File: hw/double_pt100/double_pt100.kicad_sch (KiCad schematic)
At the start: 30 parts, among them SW1 SW_Push, U1 WeMos_D1_mini, U2 OLED_091_module, U3 MAX31865_breakout, U4 MAX31865_breakout

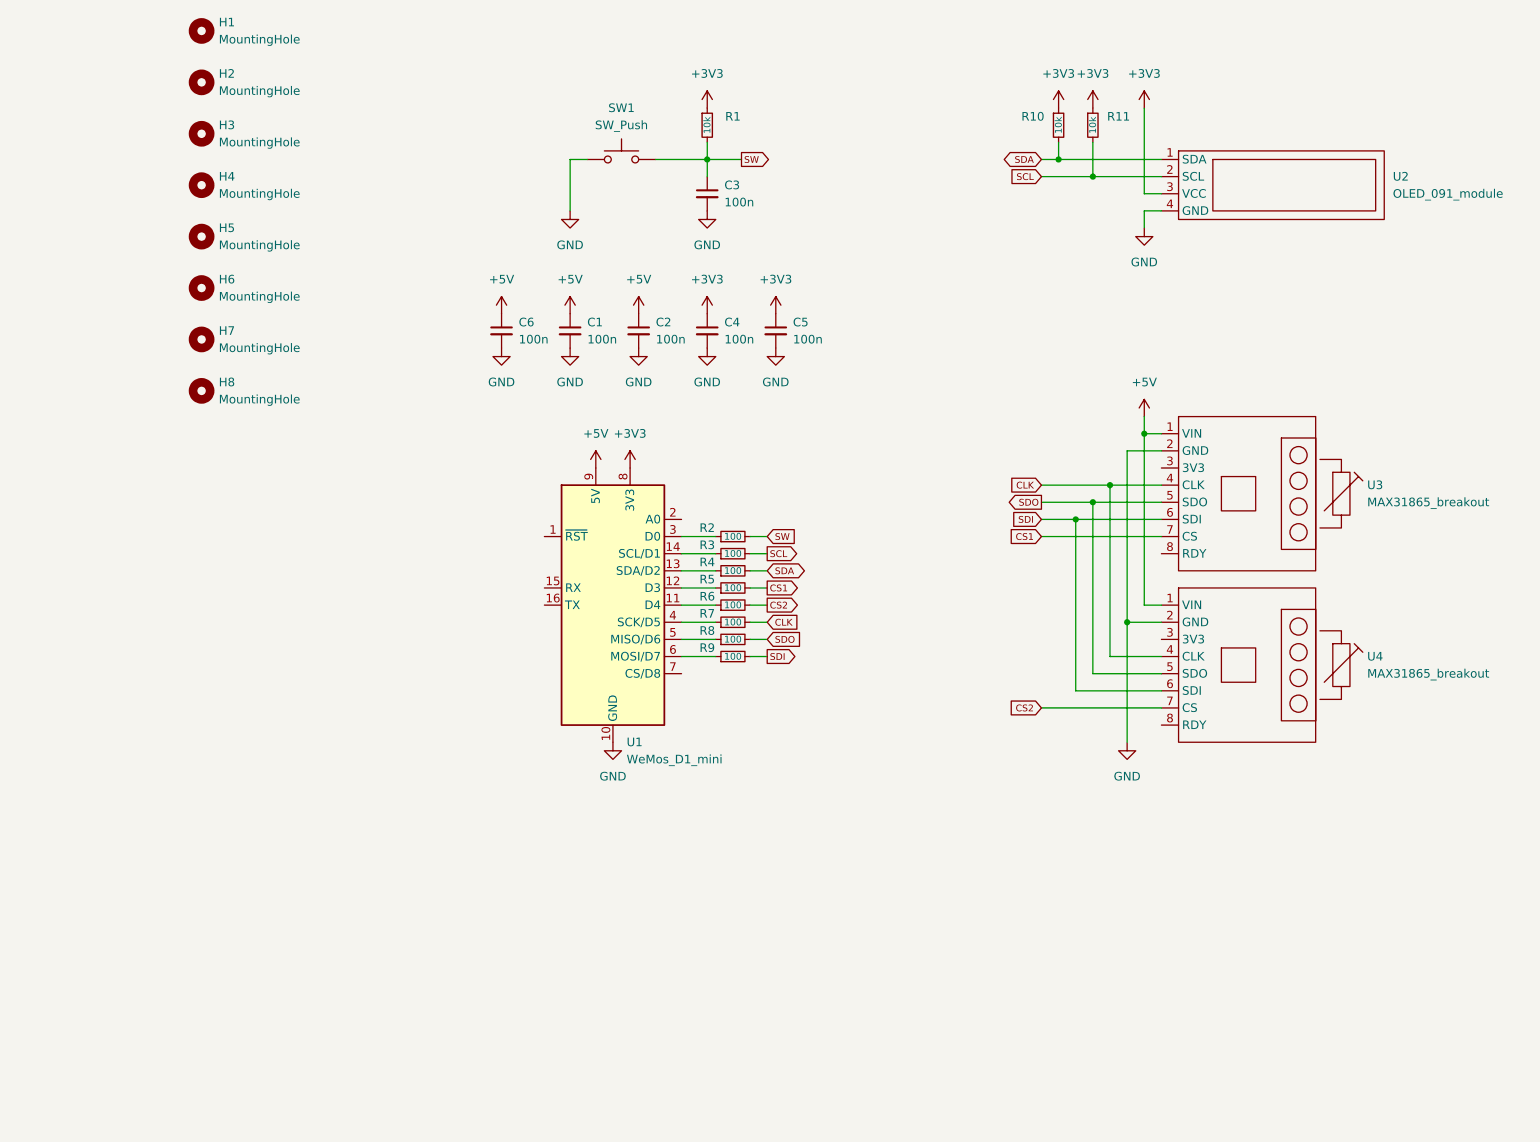
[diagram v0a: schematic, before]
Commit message: hw version 0.2 with alternative assembly
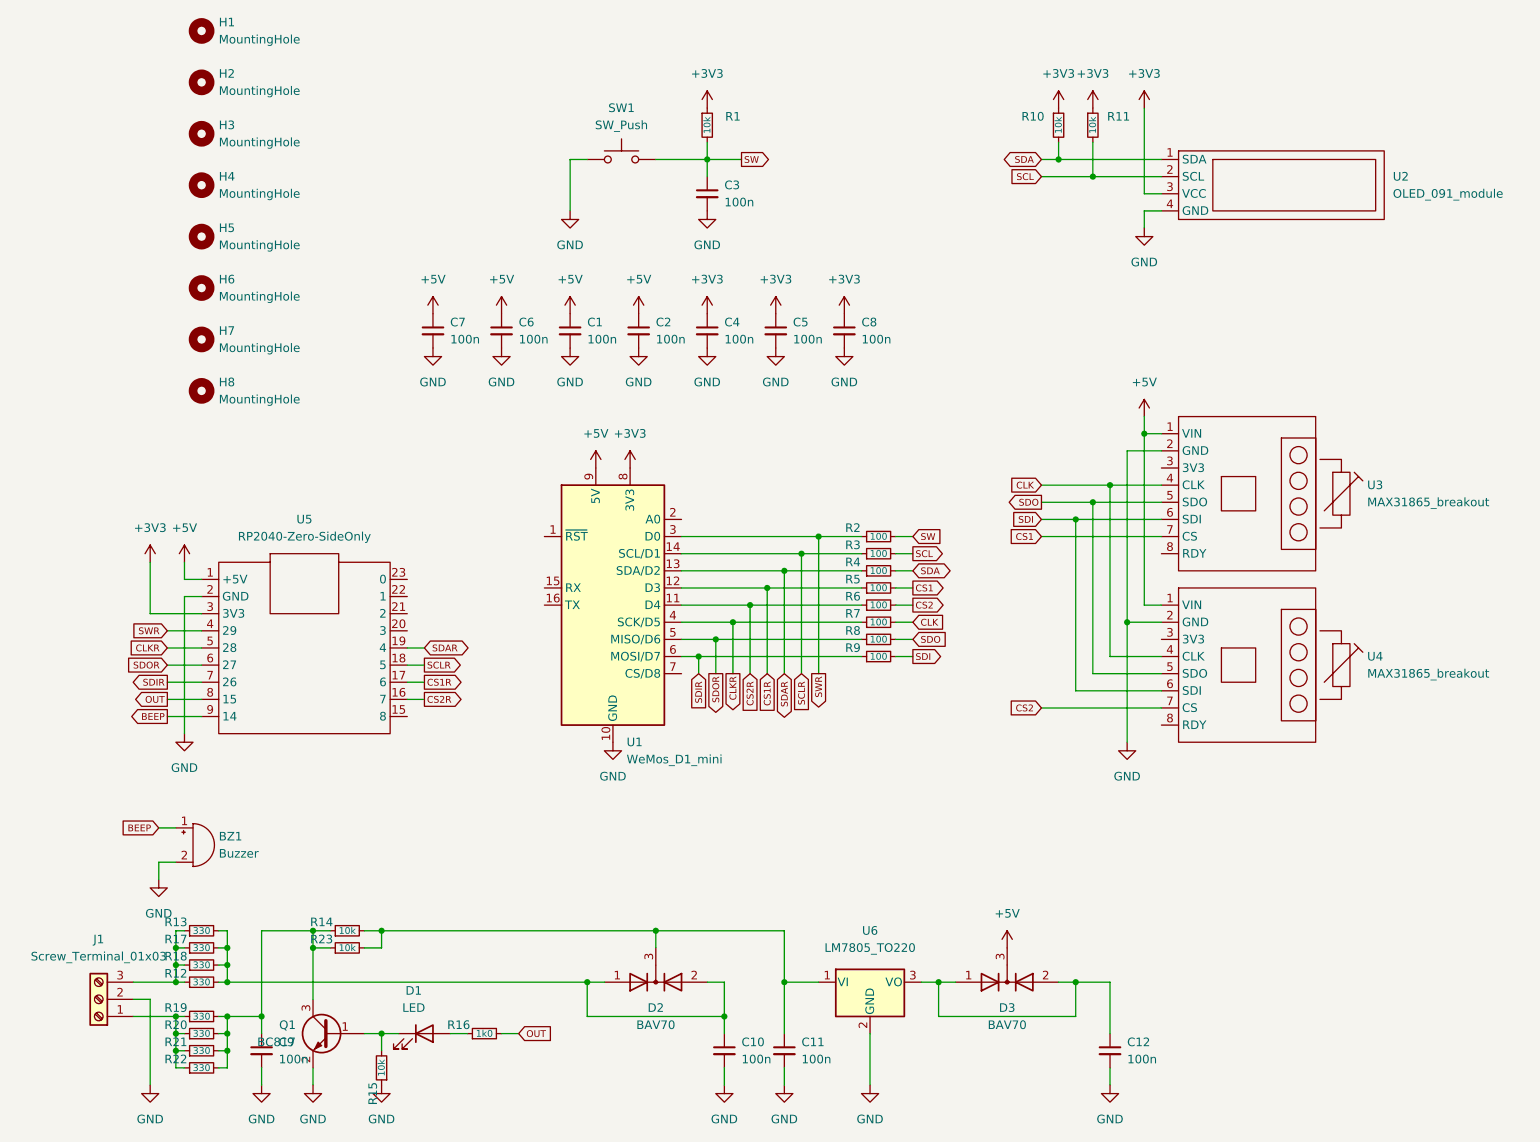
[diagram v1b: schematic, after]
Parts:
- added BZ1: Buzzer, Buzzer_Beeper:Buzzer_12x9.5RM7.6, symbol Device:Buzzer
- added C10, C11, C12, C7, C8, C9: 100n, Capacitor_SMD:C_0603_1608Metric, symbol Device:C_Small
- added D1: LED, LED_SMD:LED_0805_2012Metric, symbol Device:LED
- added D2, D3: BAV70, Package_TO_SOT_SMD:SOT-23, symbol Diode:BAV70
- added J1: Screw_Terminal_01x03, TerminalBlock:TerminalBlock_bornier-3_P5.08mm, symbol Connector:Screw_Terminal_01x03
- added Q1: BC817, Package_TO_SOT_SMD:SOT-23, symbol Transistor_BJT:BC817
- added R12, R13, R17, R18, R19, R20, R21, R22: 330, Resistor_SMD:R_0603_1608Metric, symbol Device:R_Small
- added R14, R15, R23: 10k, Resistor_SMD:R_0603_1608Metric, symbol Device:R_Small
- added R16: 1k0, Resistor_SMD:R_0603_1608Metric, symbol Device:R_Small
- added U5: RP2040-Zero-SideOnly, myModules:RP2040-Zero-SideOnly, symbol myModules:RP2040-Zero-SideOnly
- added U6: LM7805_TO220, myModules:BUCK5V, symbol Regulator_Linear:LM7805_TO220
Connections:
- net +3V3: now also C8.1, U5.3 (3V3)
- net +5V: now also C7.1, D3.3 (K), U5.1 (+5V)
- net GND: now also BZ1.2 (+), C10.2, C11.2, C12.2, C7.2, C8.2, C9.2, J1.2 (Pin_2), Q1.2 (E), R15.1, U5.2 (GND), U6.2 (GND)
- net CS1R: now reaches R5.1, U1.12 (D3)
- net CS1R: now also U5.17 (6)
- net SDIR: now reaches R9.1, U1.6 (MOSI/D7)
- net SDIR: now also U5.7 (26)
- net CLKR: now reaches R7.1, U1.4 (SCK/D5)
- net CLKR: now also U5.5 (28)
- net SWR: now reaches R2.1, U1.3 (D0)
- net SWR: now also U5.4 (29)
- net SCLR: now reaches R3.1, U1.14 (SCL/D1)
- net SCLR: now also U5.18 (5)
- net CS2R: now reaches R6.1, U1.11 (D4)
- net CS2R: now also U5.16 (7)
- net SDAR: now reaches R4.1, U1.13 (SDA/D2)
- net SDAR: now also U5.19 (4)
- net SDOR: now reaches R8.1, U1.5 (MISO/D6)
- net SDOR: now also U5.6 (27)
- new net: D1.2 (A), R16.1
- new net: J1.1 (Pin_1), R19.1, R20.1, R21.1, R22.1
- new net: C9.1, Q1.3 (C), R14.1, R19.2, R20.2, R21.2, R22.2, R23.1
- new net: J1.3 (Pin_3), R12.1, R13.1, R17.1, R18.1
- new net: C10.1, D2.1 (A), D2.2 (A), R12.2, R13.2, R17.2, R18.2
- new net: C11.1, D2.3 (K), R14.2, R23.2, U6.1 (VI)
- new net: C12.1, D3.1 (A), D3.2 (A), U6.3 (VO)
- new net: D1.1 (K), Q1.1 (B), R15.2
- new net BEEP: BZ1.1 (-), U5.9 (14)
- new net OUT: R16.2, U5.8 (15)
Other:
- moved on the sheet: R2, R3, R4, R5, R6, R7, R8, R9
